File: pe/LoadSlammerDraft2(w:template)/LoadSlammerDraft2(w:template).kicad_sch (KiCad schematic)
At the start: 23 parts, among them J1 Screw_Terminal_01x02, J2 Conn_Coaxial, J3 Conn_Coaxial, Q1 Q_NMOS_GDS, U1 UCC27511ADBV, U2 BD50FC0FP

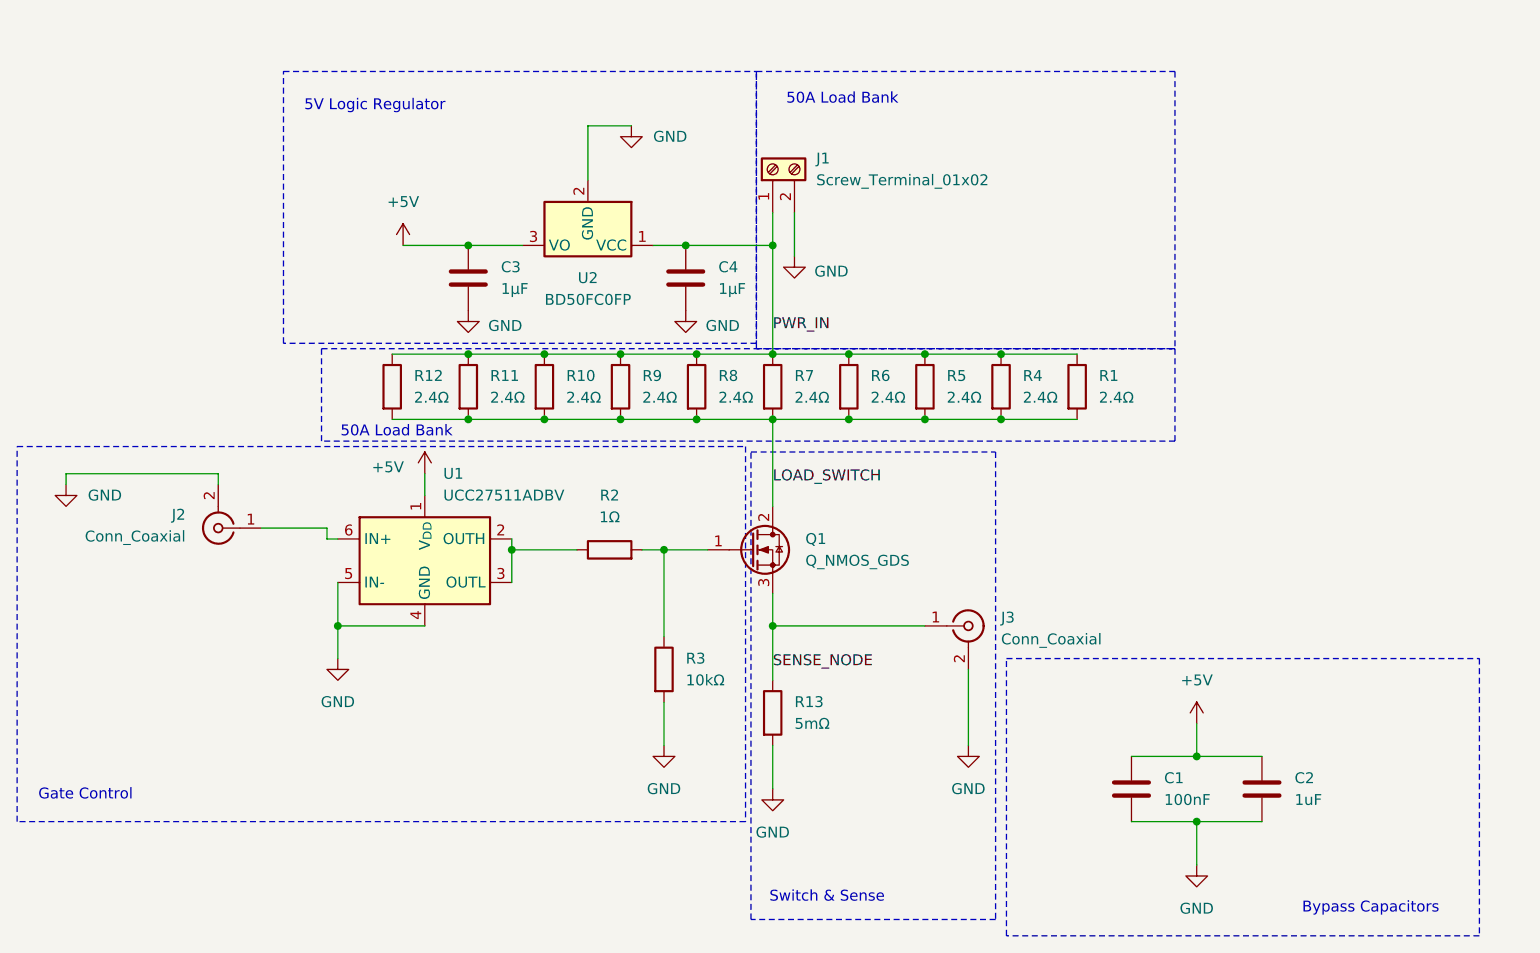
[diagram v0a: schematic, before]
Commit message: Migrated schematic to official team template
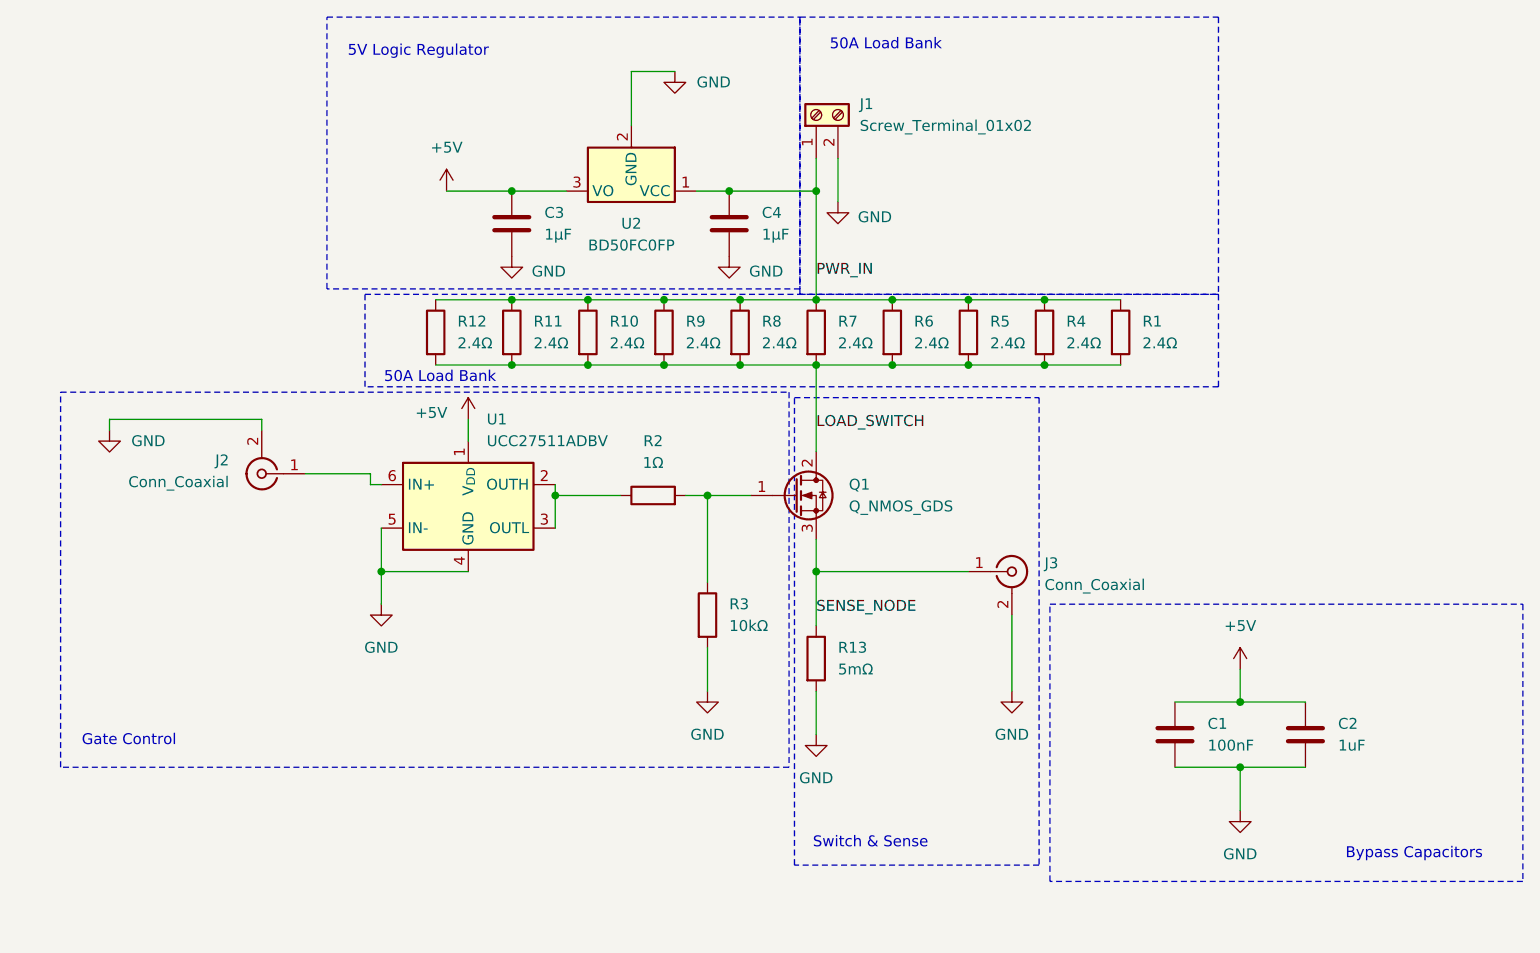
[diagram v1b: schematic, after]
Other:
- company: (none) -> Formula Slug
- title: (none) -> FS5 Load Slammer
